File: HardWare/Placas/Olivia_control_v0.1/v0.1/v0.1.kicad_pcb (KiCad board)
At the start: 2 copper layers, 100 x 100 mm, 46 parts, among them J1 PROG, J10 Motor_B, J11 I2C, J12 DAC, J13 UART2, J15 TRIAC_220VAC, J17 In12V, J2 Input1, J3 Input2, J4 Input3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

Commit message: pcb primera version
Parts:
- J1, J7: moved to B.Cu
- moved J1 6.78 mm to (130.3, 88.9)
- moved C7 3.80 mm to (134.3, 94.7), turned to 0 degrees
- moved J7 3.32 mm to (132.8, 98.5)
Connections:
- J1 pad 5: +3.3V -> +3.3V_fused
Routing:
- net +3.3V: track 271.2 -> 224.7 mm
- net GND: track 695.5 -> 732.7 mm, vias 4 -> 6
- net /TXD0: track 59.2 -> 72.7 mm, vias 1 -> 2
- net /RXD0: track 53.0 -> 61.6 mm, vias 1 -> 2
- net /EN: track 106.4 -> 99.6 mm
- net +3.3V_fused: track 133.5 -> 138.8 mm
- net /DTR: track 40.3 -> 44.9 mm, vias 1 -> 2
- net /EN_B: track 62.0 -> 59.7 mm
- net (no net): track 0.00 -> 0.05 mm, vias 0 -> 5

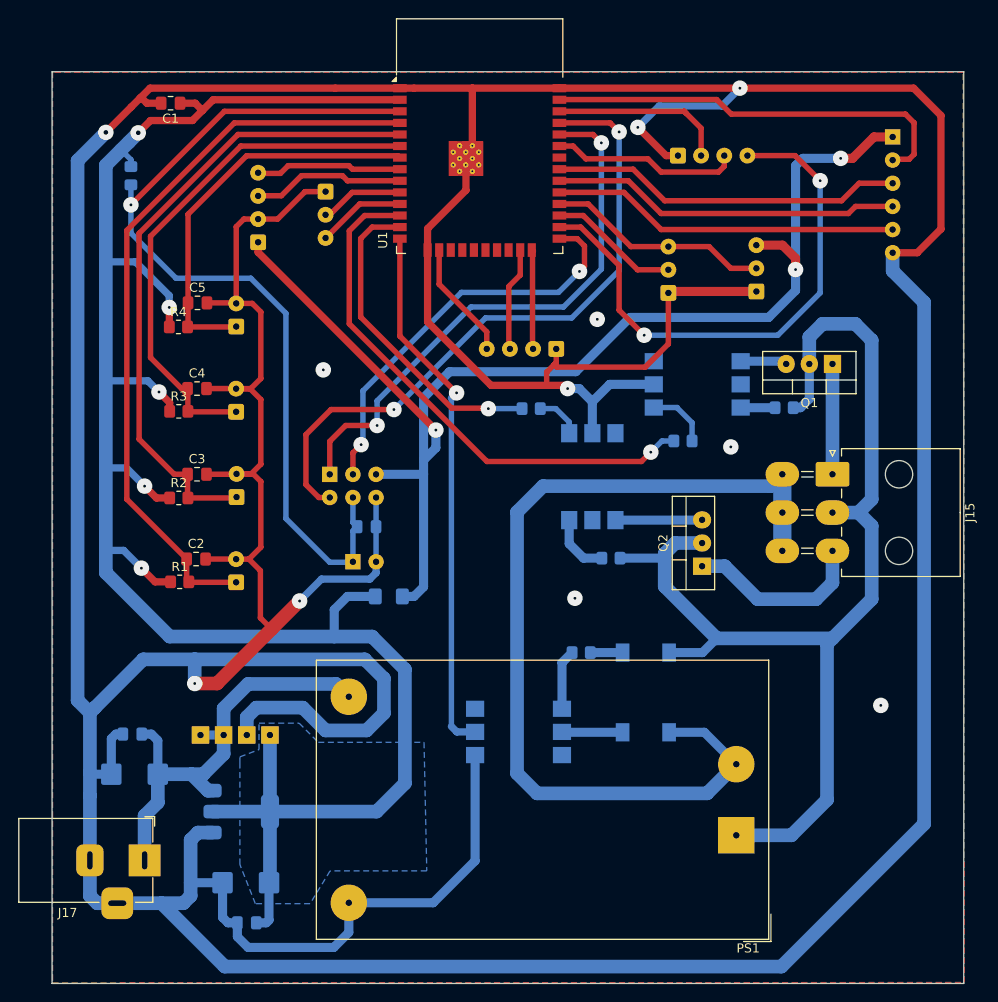
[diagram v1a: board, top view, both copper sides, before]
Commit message: pcb fix Io0 pull-up
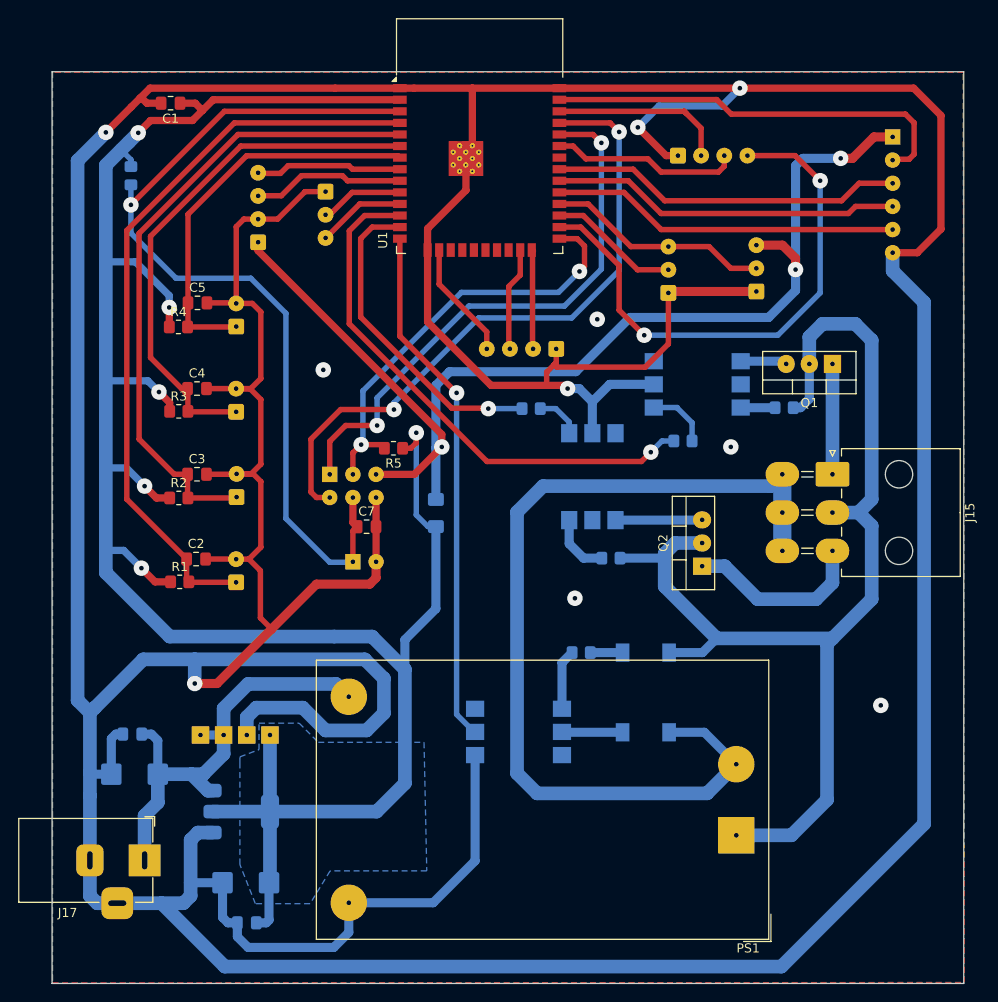
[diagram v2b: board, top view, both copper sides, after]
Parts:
- added R5: 10K, Resistor_SMD:R_0805_2012Metric_Pad1.20x1.40mm_HandSolder, F.Cu at (137.2, 86.0)
- C7: moved to F.Cu
- moved F1 10.5 mm to (141.9, 93.2), turned to 90 degrees
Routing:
- net +3.3V: track 224.7 -> 248.3 mm, vias 5 -> 6
- net +3.3V_fused: track 138.8 -> 128.1 mm
- net /DTR: track 44.9 -> 47.6 mm
- net /ZERO: track 59.2 -> 57.6 mm
- net GND: track 732.7 -> 733.1 mm, vias 6 -> 10
- net (no net): track 0.05 -> 0.00 mm, vias 5 -> 0

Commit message: minor fix routing
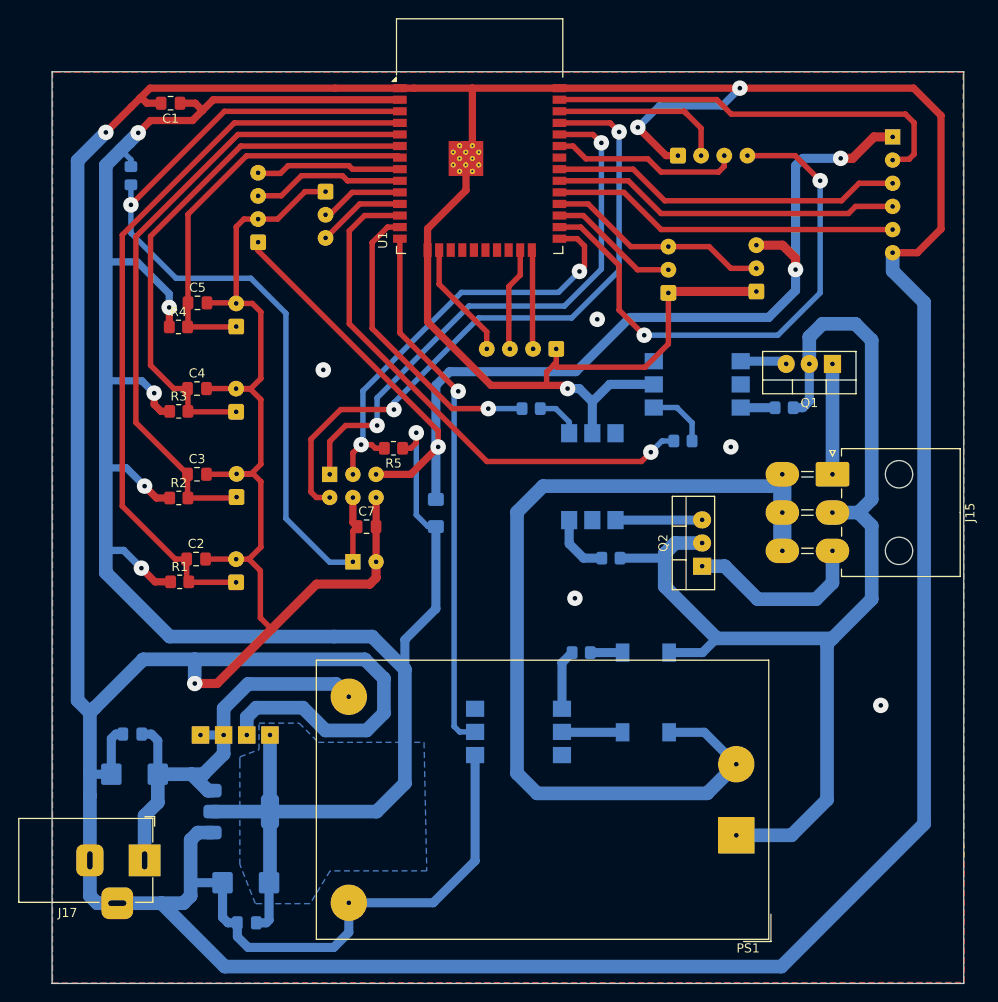
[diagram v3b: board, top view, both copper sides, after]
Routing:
- net /TRIAC_B: track 35.3 -> 33.3 mm
- net /ZERO: track 57.6 -> 58.9 mm
- net /In1: track 81.4 -> 82.6 mm
- net +3.3V_fused: track 128.1 -> 127.1 mm
- net /In2: track 70.6 -> 70.0 mm
